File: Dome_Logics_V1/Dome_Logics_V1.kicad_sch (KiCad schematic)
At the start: 26 parts, among them J1 USB_B_Micro, J12 SERIAL_FU, J2 Rear Logics, J3 Front Logics, J5 12OUT, J7 5V OUT, SW1 SW_Push, U1 ESP32-WROOM-32D_16MB_, U2 CJ2301_S1, U3 ME6211C33M5G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

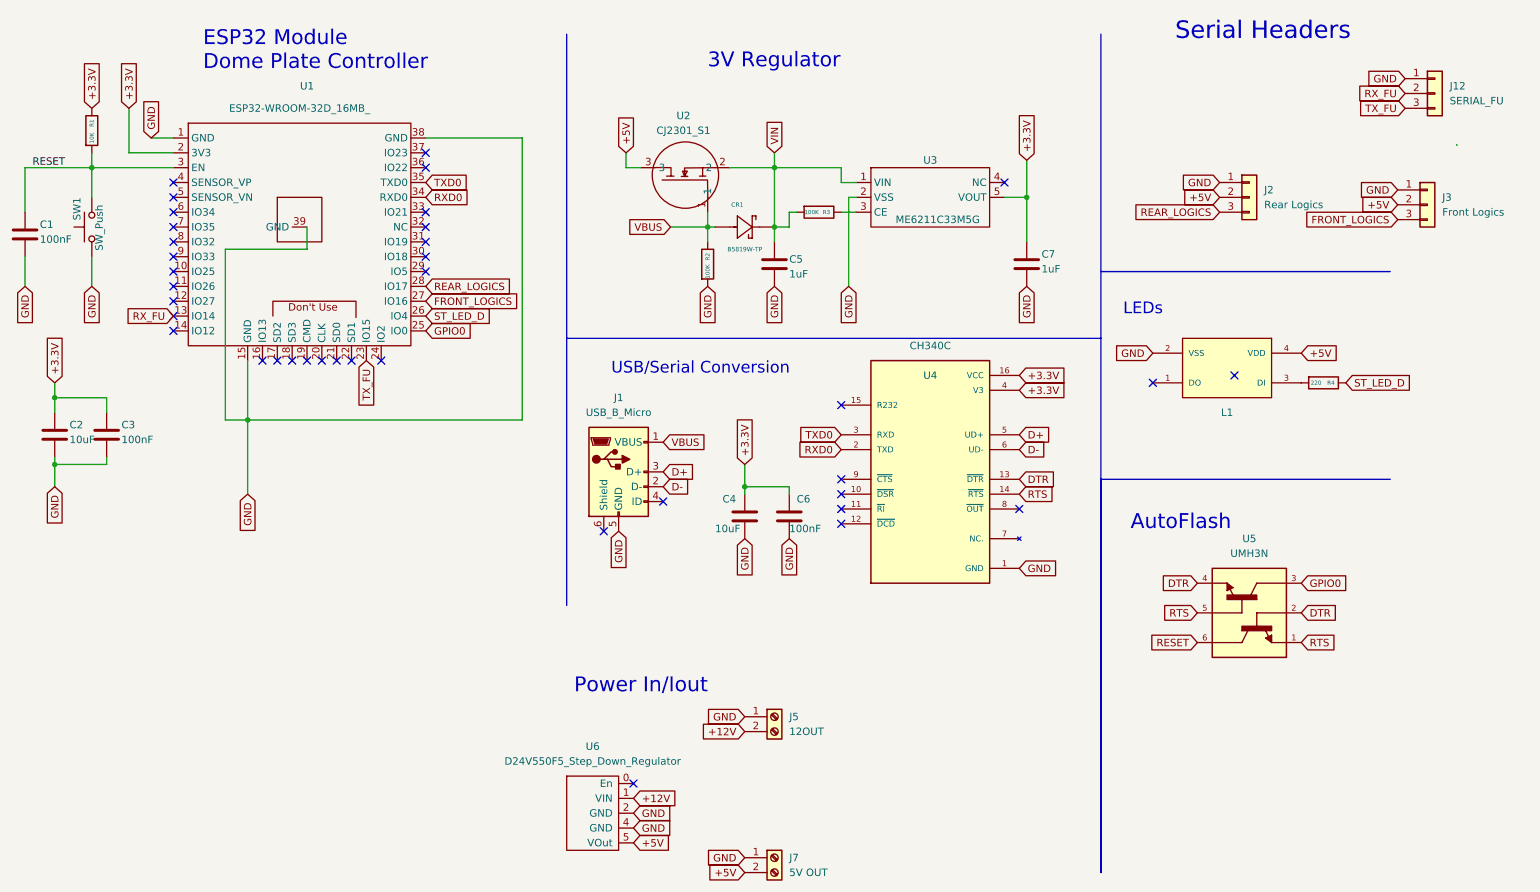
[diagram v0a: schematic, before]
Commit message: Added a 4th pin to the dome logics controller to support the curved LEDs, in case anyone wants to order them besides myself
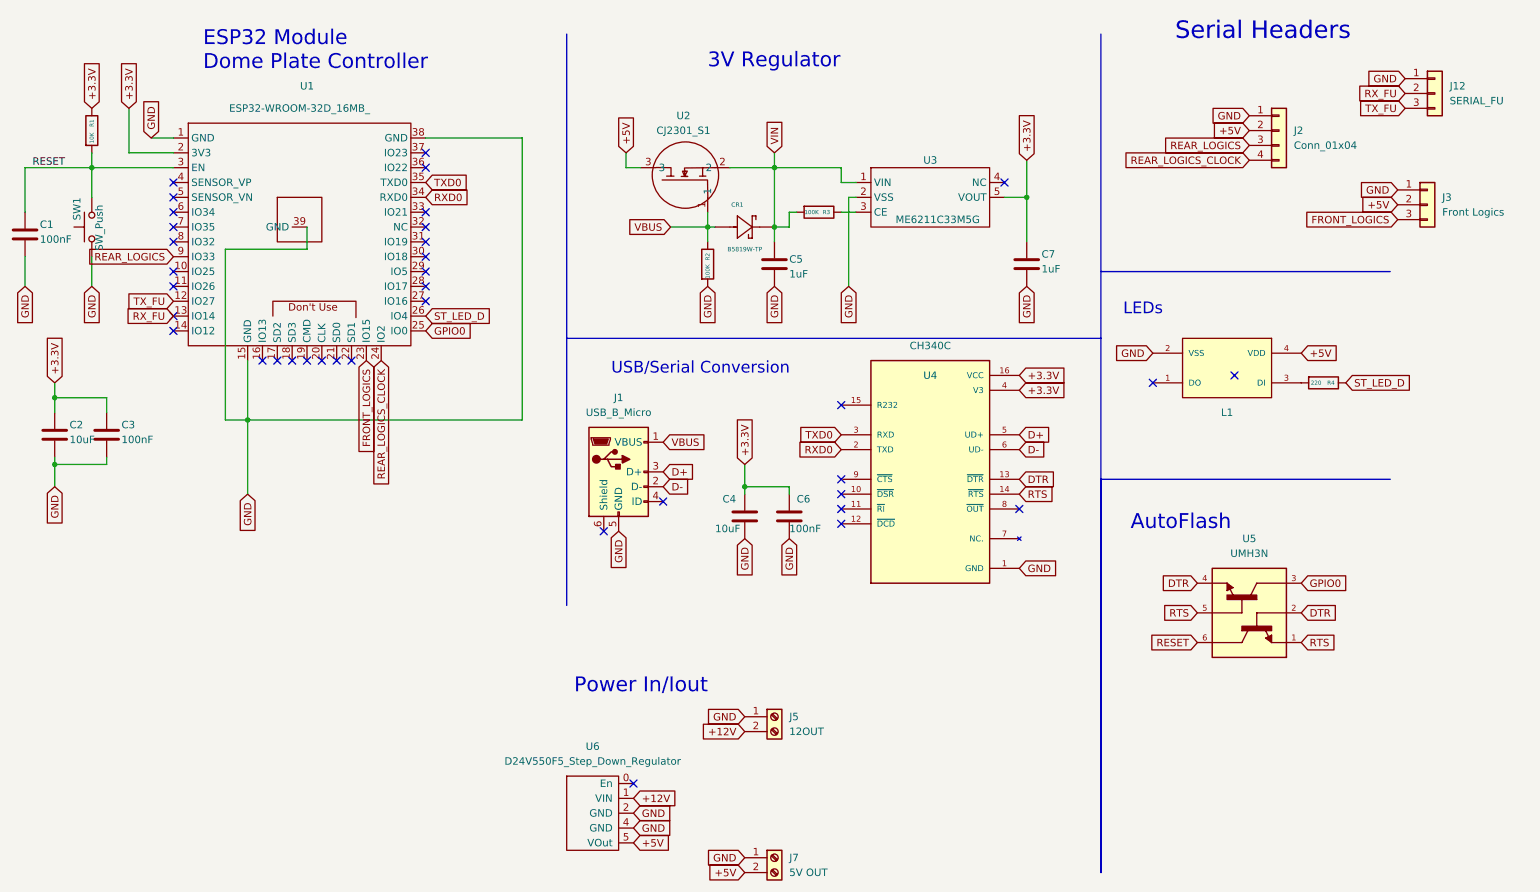
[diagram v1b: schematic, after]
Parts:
- removed J2: Rear Logics, Connector_Molex:Molex_KK-254_AE-6410-03A_1x03_P2.54mm_Vertical, symbol Connector_Generic:Conn_01x03
- added J2: Conn_01x04, Connector_Molex:Molex_KK-254_AE-6410-04A_1x04_P2.54mm_Vertical, symbol Connector_Generic:Conn_01x04
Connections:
- net +5V: now also J2.2 (Pin_2)
- net FRONT_LOGICS: now also U1.23 (IO15); no longer U1.27 (IO16)
- net GND: now also J2.1 (Pin_1)
- net REAR_LOGICS: now also U1.9 (IO33), J2.3 (Pin_3); no longer U1.28 (IO17)
- net TX_FU: now also U1.12 (IO27); no longer U1.23 (IO15)
- net REAR_LOGICS_CLOCK: now reaches U1.24 (IO2)
- net REAR_LOGICS_CLOCK: now also J2.4 (Pin_4)
- no-connect marks 38 -> 37
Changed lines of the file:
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@@
   (no_connect (at 95.25 50.8))
   (no_connect (at 52.07 43.18))
-  (no_connect (at 87.63 73.66))
   (no_connect (at 95.25 48.26))
   (no_connect (at 125.73 102.87))
@@
   (no_connect (at 219.71 77.47))
   (no_connect (at 69.85 73.66))
-  (no_connect (at 52.07 55.88))
+  (no_connect (at 95.25 60.96))
   (no_connect (at 95.25 38.1))
-  (no_connect (at 52.07 63.5))
+  (no_connect (at 95.25 63.5))
   (no_connect (at 166.37 93.98))
   (no_connect (at 166.37 96.52))
@@
     (stroke (width 0) (type default) (color 0 0 0 0))
   )
-  (wire (pts (xy 271.6847 36.6868) (xy 271.78 36.83))
-    (stroke (width 0) (type default) (color 0 0 0 0))
-  )
   (wire (pts (xy 31.75 77.47) (xy 31.75 80.01))
     (stroke (width 0) (type default) (color 0 0 0 0))
@@
     )
   )
+  (global_label "REAR_LOGICS_CLOCK" (shape input) (at 87.63 73.66 270) (fields_autoplaced)
+    (effects (font (size 1.27 1.27)) (justify right))
+    (property "Intersheet References" "${INTERSHEET_REFS}" (id 0) (at 87.5506 95.6674 90)
+      (effects (font (size 1.27 1.27)) (justify right) hide)
+    )
+  )
   (global_label "GND" (shape input) (at 48.26 35.56 90) (fields_autoplaced)
     (effects (font (size 1.27 1.27)) (justify left))
@@
     )
   )
-  (global_label "REAR_LOGICS" (shape input) (at 95.25 60.96 0) (fields_autoplaced)
-    (effects (font (size 1.27 1.27)) (justify left))
-    (property "Intersheet References" "${INTERSHEET_REFS}" (id 0) (at 110.1212 61.0394 0)
-      (effects (font (size 1.27 1.27)) (justify left) hide)
+  (global_label "REAR_LOGICS" (shape input) (at 52.07 55.88 180) (fields_autoplaced)
+    (effects (font (size 1.27 1.27)) (justify right))
+    (property "Intersheet References" "${INTERSHEET_REFS}" (id 0) (at 37.1988 55.8006 0)
+      (effects (font (size 1.27 1.27)) (justify right) hide)
     )
   )
@@
     )
   )
-  (global_label "GND" (shape input) (at 231.14 43.18 180) (fields_autoplaced)
-    (effects (font (size 1.27 1.27)) (justify right))
-    (property "Intersheet References" "${INTERSHEET_REFS}" (id 0) (at 224.9453 43.1006 0)
+  (global_label "GND" (shape input) (at 236.22 31.75 180) (fields_autoplaced)
+    (effects (font (size 1.27 1.27)) (justify right))
+    (property "Intersheet References" "${INTERSHEET_REFS}" (id 0) (at 230.0253 31.6706 0)
       (effects (font (size 1.27 1.27)) (justify right) hide)
     )
@@
     )
   )
+  (global_label "REAR_LOGICS_CLOCK" (shape input) (at 236.22 39.37 180) (fields_autoplaced)
+    (effects (font (size 1.27 1.27)) (justify right))
+    (property "Intersheet References" "${INTERSHEET_REFS}" (id 0) (at 214.2126 39.2906 0)
+      (effects (font (size 1.27 1.27)) (justify right) hide)
+    )
+  )
   (global_label "ST_LED_D" (shape input) (at 252.73 77.47 0) (fields_autoplaced)
     (effects (font (size 1.27 1.27)) (justify left))
@@
     )
   )
-  (global_label "REAR_LOGICS" (shape input) (at 231.14 48.26 180) (fields_autoplaced)
-    (effects (font (size 1.27 1.27)) (justify right))
-    (property "Intersheet References" "${INTERSHEET_REFS}" (id 0) (at 216.2688 48.1806 0)
+  (global_label "REAR_LOGICS" (shape input) (at 236.22 36.83 180) (fields_autoplaced)
+    (effects (font (size 1.27 1.27)) (justify right))
+    (property "Intersheet References" "${INTERSHEET_REFS}" (id 0) (at 221.3488 36.7506 0)
       (effects (font (size 1.27 1.27)) (justify right) hide)
     )
@@
     )
   )
-  (global_label "+5V" (shape input) (at 231.14 45.72 180) (fields_autoplaced)
-    (effects (font (size 1.27 1.27)) (justify right))
-    (property "Intersheet References" "${INTERSHEET_REFS}" (id 0) (at 224.9453 45.7994 0)
+  (global_label "+5V" (shape input) (at 236.22 34.29 180) (fields_autoplaced)
+    (effects (font (size 1.27 1.27)) (justify right))
+    (property "Intersheet References" "${INTERSHEET_REFS}" (id 0) (at 230.0253 34.3694 0)
       (effects (font (size 1.27 1.27)) (justify right) hide)
     )
@@
     )
   )
-  (global_label "FRONT_LOGICS" (shape input) (at 95.25 63.5 0) (fields_autoplaced)
-    (effects (font (size 1.27 1.27)) (justify left))
-    (property "Intersheet References" "${INTERSHEET_REFS}" (id 0) (at 111.3307 63.4206 0)
-      (effects (font (size 1.27 1.27)) (justify left) hide)
+  (global_label "FRONT_LOGICS" (shape input) (at 85.09 73.66 270) (fields_autoplaced)
+    (effects (font (size 1.27 1.27)) (justify right))
+    (property "Intersheet References" "${INTERSHEET_REFS}" (id 0) (at 85.1694 89.7407 90)
+      (effects (font (size 1.27 1.27)) (justify right) hide)
     )
   )
@@
     )
   )
-  (global_label "TX_FU" (shape input) (at 85.09 73.66 270) (fields_autoplaced)
-    (effects (font (size 1.27 1.27)) (justify right))
-    (property "Intersheet References" "${INTERSHEET_REFS}" (id 0) (at 85.0106 81.6369 90)
+  (global_label "TX_FU" (shape input) (at 52.07 63.5 180) (fields_autoplaced)
+    (effects (font (size 1.27 1.27)) (justify right))
+    (property "Intersheet References" "${INTERSHEET_REFS}" (id 0) (at 44.0931 63.4206 0)
       (effects (font (size 1.27 1.27)) (justify right) hide)
     )
@@
     (pin "2")
   )
+  (symbol (lib_id "Connector_Generic:Conn_01x04") (at 241.3 34.29 0) (unit 1)
+    (in_bom yes) (on_board yes) (fields_autoplaced)
+    (property "Reference" "J2" (id 0) (at 243.84 34.2899 0)
+      (effects (font (size 1.27 1.27)) (justify left))
+    )
+    (property "Value" "Conn_01x04" (id 1) (at 243.84 36.8299 0)
+      (effects (font (size 1.27 1.27)) (justify left))
+    )
+    (property "Footprint" "Connector_Molex:Molex_KK-254_AE-6410-04A_1x04_P2.54mm_Vertical" (id 2) (at 241.3 34.29 0)
+      (effects (font (size 1.27 1.27)) hide)
+    )
+    (property "Datasheet" "~" (id 3) (at 241.3 34.29 0)
+      (effects (font (size 1.27 1.27)) hide)
+    )
+    (pin "1")
+    (pin "2")
+    (pin "3")
+    (pin "4")
+  )
   (symbol (lib_id "Device:C") (at 40.64 86.36 0) (unit 1)
     (in_bom yes) (on_board yes) (fields_autoplaced)
@@
     )
     (property "LCSC" "C471416" (id 4) (at 267.97 27.94 0)
-      (effects (font (size 1.27 1.27)) hide)
-    )
-    (pin "1")
-    (pin "2")
-    (pin "3")
-  )
-  (symbol (lib_id "Connector_Generic:Conn_01x03") (at 236.22 45.72 0) (unit 1)
-    (in_bom yes) (on_board yes)
-    (property "Reference" "J2" (id 0) (at 238.76 44.4499 0)
-      (effects (font (size 1.27 1.27)) (justify left))
-    )
-    (property "Value" "Rear Logics" (id 1) (at 238.76 46.9899 0)
-      (effects (font (size 1.27 1.27)) (justify left))
-    )
-    (property "Footprint" "Connector_Molex:Molex_KK-254_AE-6410-03A_1x03_P2.54mm_Vertical" (id 2) (at 236.22 45.72 0)
-      (effects (font (size 1.27 1.27)) hide)
-    )
-    (property "Datasheet" "~" (id 3) (at 236.22 45.72 0)
-      (effects (font (size 1.27 1.27)) hide)
-    )
-    (property "LCSC" "C471416" (id 4) (at 236.22 45.72 0)
       (effects (font (size 1.27 1.27)) hide)
     )
@@
       (reference "J1") (unit 1) (value "USB_B_Micro") (footprint "Connector_USB:USB_Micro-B_Amphenol_10118194_Horizontal")
     )
-    (path "/7ec600ca-73c6-4bde-8d22-fdcefc6104ea"
-      (reference "J2") (unit 1) (value "Rear Logics") (footprint "Connector_Molex:Molex_KK-254_AE-6410-03A_1x03_P2.54mm_Vertical")
+    (path "/227dd642-8636-46aa-b8b3-4d504267ff11"
+      (reference "J2") (unit 1) (value "Conn_01x04") (footprint "Connector_Molex:Molex_KK-254_AE-6410-04A_1x04_P2.54mm_Vertical")
     )
     (path "/57cb0358-c950-4330-b4ba-f2b303d64926"
